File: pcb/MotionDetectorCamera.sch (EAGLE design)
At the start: 134 parts, among them J2 S-MOUNT-LENS-HOLDER, J3 MINI-USB-JACK, U1 LATTICE-ICE40HX4K-BG121, U10 NXP-NTB0102, U11 ON-NLAS3157, U12 ON-NLAS3157, U13 STM-STM32F730, U2 TI-TPS6280XYKAR, U22 TI-TPD4S012DRYR, U3 MICROSD-SOCKET, U4 TI-TPS6280XYKAR, U5 W989D6DBGX6I, U6 TI-TPS63805YFFR, U8 ON-AR0330CS1C12SPKA0, U9 TI-TMUX1574, X1 SITIME-SIT8021, X2 SITIME-SIT8021

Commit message: Add vias around ground pads
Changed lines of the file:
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@@
 <instances>
 <instance part="J3" gate="G$1" x="5.08" y="-5.08" smashed="yes">
-<attribute name="NAME" x="5.08" y="-4.318" size="1.778" layer="95"/>
+<attribute name="NAME" x="5.08" y="-2.54" size="1.778" layer="95" align="top-left"/>
 </instance>
 <instance part="FB10" gate="G$1" x="43.18" y="-7.62" smashed="yes">

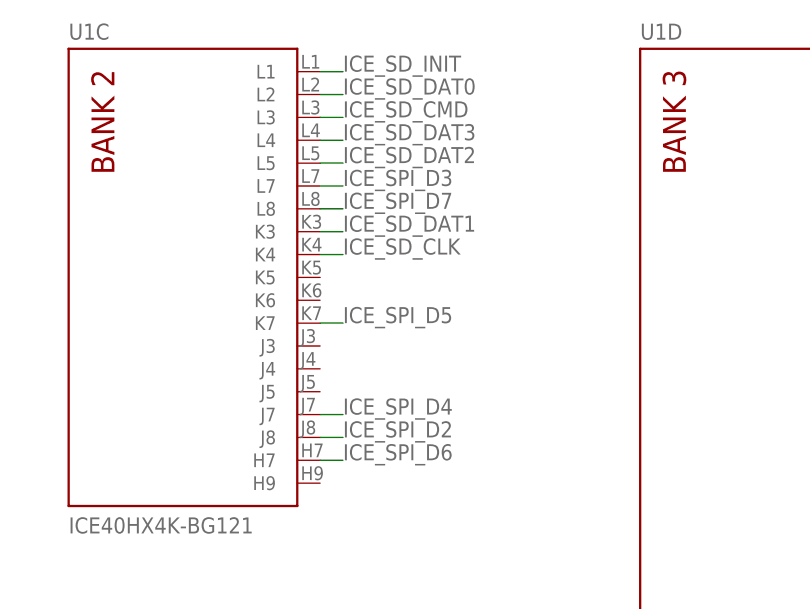
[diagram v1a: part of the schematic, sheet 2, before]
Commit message: Finished length matching QUADSPI lines
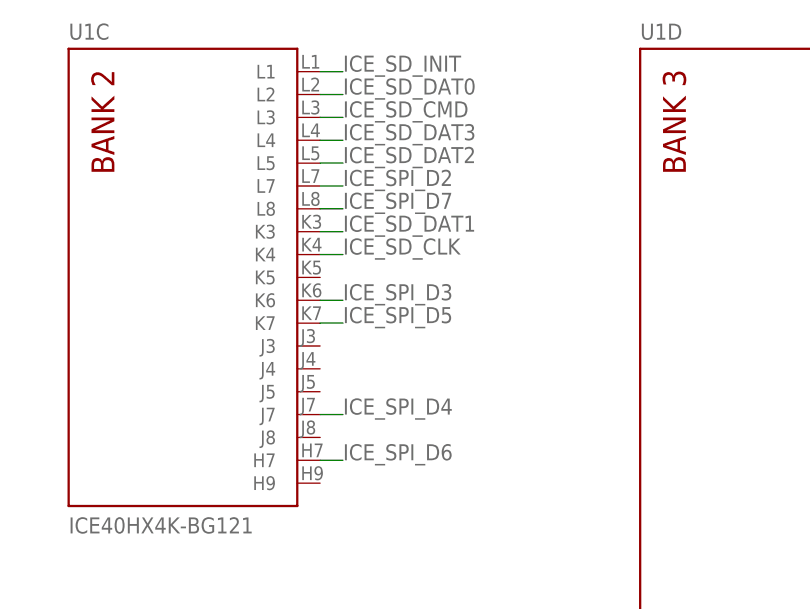
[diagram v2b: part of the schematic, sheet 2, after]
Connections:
- net ICE_SPI_D2: now also U13F.PF7_K1, U1C.L7; no longer U13E.PE2_A2, U1C.J8
- net ICE_SPI_D3: now also U1C.K6; no longer U1C.L7
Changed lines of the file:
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@@
 <net name="ICE_SPI_D2" class="0">
 <segment>
-<pinref part="U1" gate="C" pin="J8"/>
-<wire x1="149.86" y1="25.4" x2="152.4" y2="25.4" width="0.1524" layer="91"/>
-<label x="152.4" y="25.4" size="1.778" layer="95"/>
+<wire x1="149.86" y1="53.34" x2="152.4" y2="53.34" width="0.1524" layer="91"/>
+<label x="152.4" y="53.34" size="1.778" layer="95"/>
+<pinref part="U1" gate="C" pin="L7"/>
 </segment>
 </net>
@@
 <net name="ICE_SPI_D3" class="0">
 <segment>
-<pinref part="U1" gate="C" pin="L7"/>
-<wire x1="149.86" y1="53.34" x2="152.4" y2="53.34" width="0.1524" layer="91"/>
-<label x="152.4" y="53.34" size="1.778" layer="95"/>
+<wire x1="149.86" y1="40.64" x2="152.4" y2="40.64" width="0.1524" layer="91"/>
+<label x="152.4" y="40.64" size="1.778" layer="95"/>
+<pinref part="U1" gate="C" pin="K6"/>
 </segment>
 </net>
@@
 <net name="ICE_SPI_D2" class="0">
 <segment>
-<pinref part="U13" gate="E" pin="PE2_A2"/>
-<wire x1="27.94" y1="-78.74" x2="30.48" y2="-78.74" width="0.1524" layer="91"/>
-<label x="30.48" y="-78.74" size="1.778" layer="95"/>
-</segment>
-</net>
+<pinref part="U13" gate="F" pin="PF7_K1"/>
+<wire x1="68.58" y1="-91.44" x2="71.12" y2="-91.44" width="0.1524" layer="91"/>
+<label x="71.12" y="-91.44" size="1.778" layer="95"/>
+</segment>
+</net>

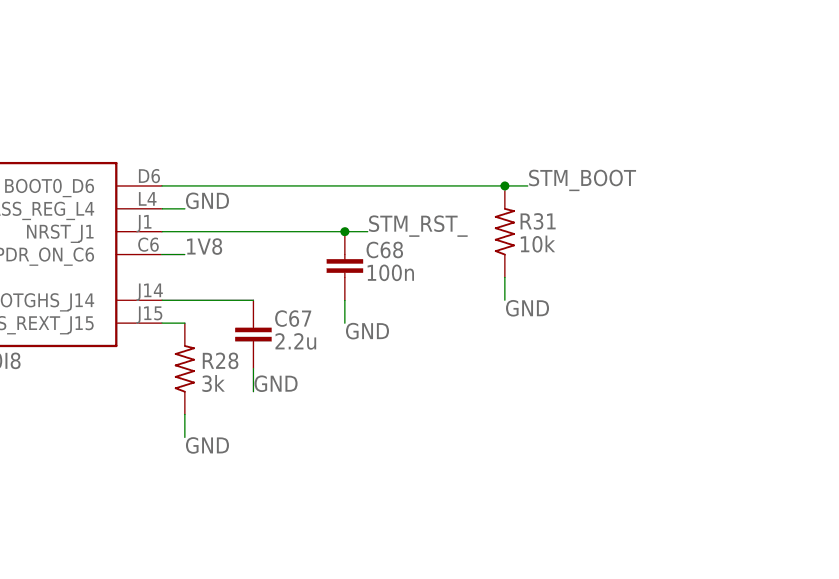
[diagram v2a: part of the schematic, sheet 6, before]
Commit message: Added part numbers. Committing before swapping out poor capacitors for better ones.
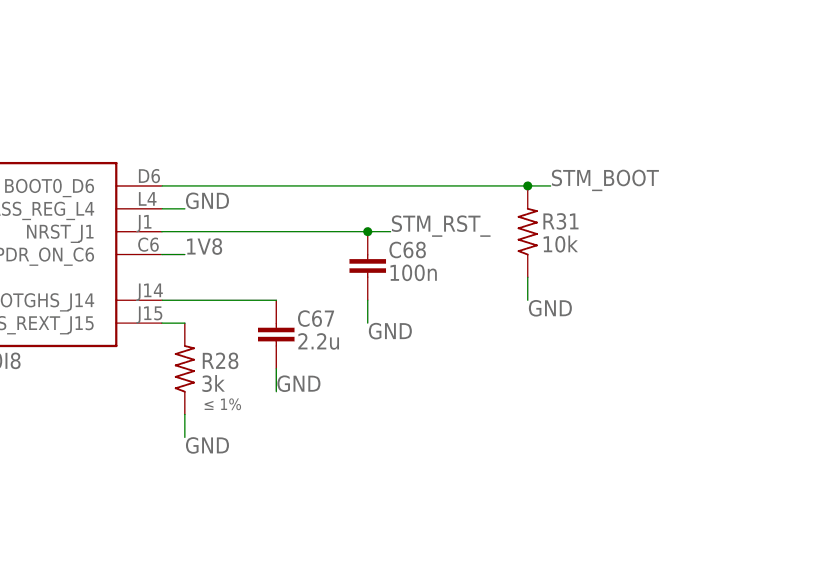
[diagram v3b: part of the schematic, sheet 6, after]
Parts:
- J2: MFG (none) -> Marshall Electronics; PN (none) -> V-LH4
- R28: MFG (none) -> Yageo; PN (none) -> AC0402FR-073KL
- R30: MFG (none) -> Vishay; PN (none) -> CRCW04024K70FKEDC
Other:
- note added: "≤ 1%"
- moved on the sheet: C67, C68, R31
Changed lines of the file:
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@@
 <part name="TP8" library="EagleLibrary" deviceset="TEST-POINT" device=""/>
 <part name="TP9" library="EagleLibrary" deviceset="TEST-POINT" device=""/>
-<part name="J2" library="EagleLibrary" deviceset="S-MOUNT-LENS-HOLDER" device=""/>
+<part name="J2" library="EagleLibrary" deviceset="S-MOUNT-LENS-HOLDER" device="">
+<attribute name="MFG" value="Marshall Electronics"/>
+<attribute name="PN" value="V-LH4"/>
+</part>
 <part name="U9" library="EagleLibrary" deviceset="TI-TMUX1574" device=""/>
 <part name="U10" library="EagleLibrary" deviceset="NXP-NTB0102" device=""/>
@@
 </part>
 <part name="R28" library="EagleLibrary" deviceset="RESISTOR" device="0402" value="3k">
-<attribute name="MFG" value=""/>
-<attribute name="PN" value=""/>
+<attribute name="MFG" value="Yageo"/>
+<attribute name="PN" value="AC0402FR-073KL"/>
 </part>
 <part name="C68" library="EagleLibrary" deviceset="CAPACITOR" device="0402" value="100n">
@@
 </part>
 <part name="R30" library="EagleLibrary" deviceset="RESISTOR" device="0402" value="4.7k">
-<attribute name="MFG" value=""/>
-<attribute name="PN" value=""/>
+<attribute name="MFG" value="Vishay"/>
+<attribute name="PN" value="CRCW04024K70FKEDC"/>
 </part>
 <part name="J3" library="EagleLibrary" deviceset="MINI-USB-JACK" device=""/>
@@
 <instance part="J2" gate="G$1" x="134.62" y="-5.08" smashed="yes">
 <attribute name="NAME" x="134.62" y="-4.318" size="1.778" layer="95"/>
+<attribute name="MFG" x="134.62" y="-5.08" size="1.778" layer="96" display="off"/>
+<attribute name="PN" x="134.62" y="-5.08" size="1.778" layer="96" display="off"/>
 </instance>
 <instance part="R30" gate="G$1" x="116.84" y="50.8" smashed="yes" rot="R270">
@@
 <wire x1="81.28" y1="-251.46" x2="81.28" y2="-233.68" width="0.1524" layer="95"/>
 <wire x1="81.28" y1="-233.68" x2="48.26" y2="-233.68" width="0.1524" layer="95"/>
+<text x="83.312" y="-163.322" size="1.27" layer="95" align="top-left">≤ 1%</text>
 </plain>
 <instances>
@@
 <attribute name="MFG" x="68.58" y="-241.3" size="1.778" layer="96" display="off"/>
 </instance>
-<instance part="C67" gate="G$1" x="88.9" y="-154.94" smashed="yes">
-<attribute name="PN" x="88.9" y="-154.94" size="1.778" layer="96" display="off"/>
-<attribute name="NAME" x="91.186" y="-155.321" size="1.778" layer="95"/>
-<attribute name="VALUE" x="91.186" y="-157.861" size="1.778" layer="96"/>
-<attribute name="MFG" x="88.9" y="-154.94" size="1.778" layer="96" display="off"/>
+<instance part="C67" gate="G$1" x="91.44" y="-154.94" smashed="yes">
+<attribute name="PN" x="91.44" y="-154.94" size="1.778" layer="96" display="off"/>
+<attribute name="NAME" x="93.726" y="-155.321" size="1.778" layer="95"/>
+<attribute name="VALUE" x="93.726" y="-157.861" size="1.778" layer="96"/>
+<attribute name="MFG" x="91.44" y="-154.94" size="1.778" layer="96" display="off"/>
 </instance>
 <instance part="R28" gate="G$1" x="81.28" y="-160.02" smashed="yes" rot="R90">
@@
 <attribute name="PN" x="81.28" y="-160.02" size="1.778" layer="96" rot="R90" display="off"/>
 </instance>
-<instance part="C68" gate="G$1" x="99.06" y="-147.32" smashed="yes">
-<attribute name="PN" x="99.06" y="-147.32" size="1.778" layer="96" display="off"/>
-<attribute name="NAME" x="101.346" y="-147.701" size="1.778" layer="95"/>
-<attribute name="VALUE" x="101.346" y="-150.241" size="1.778" layer="96"/>
-<attribute name="MFG" x="99.06" y="-147.32" size="1.778" layer="96" display="off"/>
-</instance>
-<instance part="R31" gate="G$1" x="116.84" y="-144.78" smashed="yes" rot="R90">
-<attribute name="NAME" x="118.364" y="-142.748" size="1.778" layer="95" align="top-left"/>
-<attribute name="VALUE" x="118.364" y="-145.288" size="1.778" layer="96" align="top-left"/>
-<attribute name="MFG" x="116.84" y="-144.78" size="1.778" layer="96" rot="R90" display="off"/>
-<attribute name="PN" x="116.84" y="-144.78" size="1.778" layer="96" rot="R90" display="off"/>
+<instance part="C68" gate="G$1" x="101.6" y="-147.32" smashed="yes">
+<attribute name="PN" x="101.6" y="-147.32" size="1.778" layer="96" display="off"/>
+<attribute name="NAME" x="103.886" y="-147.701" size="1.778" layer="95"/>
+<attribute name="VALUE" x="103.886" y="-150.241" size="1.778" layer="96"/>
+<attribute name="MFG" x="101.6" y="-147.32" size="1.778" layer="96" display="off"/>
+</instance>
+<instance part="R31" gate="G$1" x="119.38" y="-144.78" smashed="yes" rot="R90">
+<attribute name="NAME" x="120.904" y="-142.748" size="1.778" layer="95" align="top-left"/>
+<attribute name="VALUE" x="120.904" y="-145.288" size="1.778" layer="96" align="top-left"/>
+<attribute name="MFG" x="119.38" y="-144.78" size="1.778" layer="96" rot="R90" display="off"/>
+<attribute name="PN" x="119.38" y="-144.78" size="1.778" layer="96" rot="R90" display="off"/>
 </instance>
 <instance part="C61" gate="G$1" x="226.06" y="-22.86" smashed="yes">
@@
 <segment>
 <pinref part="C67" gate="G$1" pin="2"/>
-<wire x1="88.9" y1="-160.02" x2="88.9" y2="-162.56" width="0.1524" layer="91"/>
-<label x="88.9" y="-162.56" size="1.778" layer="95"/>
+<wire x1="91.44" y1="-160.02" x2="91.44" y2="-162.56" width="0.1524" layer="91"/>
+<label x="91.44" y="-162.56" size="1.778" layer="95"/>
 </segment>
 <segment>
@@
 <segment>
 <pinref part="C68" gate="G$1" pin="2"/>
-<wire x1="99.06" y1="-152.4" x2="99.06" y2="-154.94" width="0.1524" layer="91"/>
-<label x="99.06" y="-154.94" size="1.778" layer="95" align="top-left"/>
+<wire x1="101.6" y1="-152.4" x2="101.6" y2="-154.94" width="0.1524" layer="91"/>
+<label x="101.6" y="-154.94" size="1.778" layer="95" align="top-left"/>
 </segment>
 <segment>
 <pinref part="R31" gate="G$1" pin="1"/>
-<wire x1="116.84" y1="-149.86" x2="116.84" y2="-152.4" width="0.1524" layer="91"/>
-<label x="116.84" y="-152.4" size="1.778" layer="95" align="top-left"/>
+<wire x1="119.38" y1="-149.86" x2="119.38" y2="-152.4" width="0.1524" layer="91"/>
+<label x="119.38" y="-152.4" size="1.778" layer="95" align="top-left"/>
 </segment>
 <segment>
@@
 <segment>
 <pinref part="U13" gate="J" pin="NRST_J1"/>
-<wire x1="78.74" y1="-144.78" x2="99.06" y2="-144.78" width="0.1524" layer="91"/>
+<wire x1="78.74" y1="-144.78" x2="101.6" y2="-144.78" width="0.1524" layer="91"/>
 <pinref part="C68" gate="G$1" pin="1"/>
-<wire x1="99.06" y1="-144.78" x2="101.6" y2="-144.78" width="0.1524" layer="91"/>
-<junction x="99.06" y="-144.78"/>
-<label x="101.6" y="-144.78" size="1.778" layer="95"/>
+<wire x1="101.6" y1="-144.78" x2="104.14" y2="-144.78" width="0.1524" layer="91"/>
+<junction x="101.6" y="-144.78"/>
+<label x="104.14" y="-144.78" size="1.778" layer="95"/>
 </segment>
 <segment>
@@
 <pinref part="U13" gate="J" pin="BOOT0_D6"/>
 <pinref part="R31" gate="G$1" pin="2"/>
-<wire x1="78.74" y1="-139.7" x2="116.84" y2="-139.7" width="0.1524" layer="91"/>
-<label x="119.38" y="-139.7" size="1.778" layer="95"/>
-<wire x1="116.84" y1="-139.7" x2="119.38" y2="-139.7" width="0.1524" layer="91"/>
-<junction x="116.84" y="-139.7"/>
+<wire x1="78.74" y1="-139.7" x2="119.38" y2="-139.7" width="0.1524" layer="91"/>
+<label x="121.92" y="-139.7" size="1.778" layer="95"/>
+<wire x1="119.38" y1="-139.7" x2="121.92" y2="-139.7" width="0.1524" layer="91"/>
+<junction x="119.38" y="-139.7"/>
 </segment>
 <segment>
@@
 <pinref part="C67" gate="G$1" pin="1"/>
 <pinref part="U13" gate="J" pin="VDD12OTGHS_J14"/>
-<wire x1="88.9" y1="-152.4" x2="78.74" y2="-152.4" width="0.1524" layer="91"/>
+<wire x1="91.44" y1="-152.4" x2="78.74" y2="-152.4" width="0.1524" layer="91"/>
 </segment>
 </net>
